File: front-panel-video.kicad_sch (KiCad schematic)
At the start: 0 parts

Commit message: [#81876] Add power section
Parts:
- added J2: DisplayPort-Mini_TE_2129320-3, antmicro-footprints:DisplayPort-Mini_Receptacle_TE_2129320-3, symbol antmicroVideoConnectors:DisplayPort-Mini_TE_2129320-3
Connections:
- new net: J2.1 (GND), J2.13 (GND), J2.14 (GND), J2.19 (GND), J2.7 (GND), J2.8 (GND)
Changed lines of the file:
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@@
+		)
+	)
+	(symbol
+		(lib_id "antmicroVideoConnectors:DisplayPort-Mini_TE_2129320-3")
+		(at 153.67 90.17 0)
+		(unit 1)
+		(exclude_from_sim no)
+		(in_bom yes)
+		(on_board yes)
+		(dnp no)
+		(fields_autoplaced yes)
+		(property "Reference" "J2"
+			(at 166.4335 82.55 0)
+			(effects
+				(font
+					(size 1.27 1.27)
+					(thickness 0.15)
+				)
+			)
+		)
+		(property "Value" "DisplayPort-Mini_TE_2129320-3"
+			(at 199.39 90.17 0)
+			(effects
+				(font
+					(size 1.27 1.27)
+					(thickness 0.15)
+				)
+				(justify left bottom)
+				(hide yes)
+			)
+		)
+		(property "Footprint" "antmicro-footprints:DisplayPort-Mini_Receptacle_TE_2129320-3"
+			(at 199.39 92.71 0)
+			(effects
+				(font
+					(size 1.27 1.27)
+					(thickness 0.15)
+				)
+				(justify left bottom)
+				(hide yes)
+			)
+		)
+		(property "Datasheet" "https://www.te.com/usa-en/product-2129320-3.html"
+			(at 199.39 95.25 0)
+			(effects
+				(font
+					(size 1.27 1.27)
+					(thickness 0.15)
+				)
+				(justify left bottom)
+				(hide yes)
+			)
+		)
+		(property "Description" "DisplayPort, Mini Receptacle Connector 20 Position Through Hole, Right Angle"
+			(at 153.67 90.17 0)
+			(effects
+				(font
+					(size 1.27 1.27)
+				)
+				(hide yes)
+			)
+		)
+		(property "MPN" "2129320-3"
+			(at 166.4335 85.09 0)
+			(effects
+				(font
+					(size 1.27 1.27)
+					(thickness 0.15)
+				)
+			)
+		)
+		(property "Manufacturer" "TE Connectivity"
+			(at 199.39 100.33 0)
+			(effects
+				(font
+					(size 1.27 1.27)
+					(thickness 0.15)
+				)
+				(justify left bottom)
+				(hide yes)
+			)
+		)
+		(property "Author" "Antmicro"
+			(at 199.39 102.87 0)
+			(effects
+				(font
+					(size 1.27 1.27)
+					(thickness 0.15)
+				)
+				(justify left bottom)
+				(hide yes)
+			)
+		)
+		(property "License" "Apache-2.0"
+			(at 199.39 105.41 0)
+			(effects
+				(font
+					(size 1.27 1.27)
+					(thickness 0.15)
+				)
+				(justify left bottom)
+				(hide yes)
+			)
+		)
+		(pin "5"
+		)
+		(pin "SH"
+		)
+		(pin "8"
+		)
+		(pin "13"
+		)
+		(pin "19"
+		)
+		(pin "16"
+		)
+		(pin "20"
+		)
+		(pin "15"
+		)
+		(pin "6"
+		)
+		(pin "1"
+		)
+		(pin "11"
+		)
+		(pin "7"
+		)
+		(pin "17"
+		)
+		(pin "14"
+		)
+		(pin "4"
+		)
+		(pin "10"
+		)
+		(pin "2"
+		)
+		(pin "9"
+		)
+		(pin "12"
+		)
+		(pin "18"
+		)
+		(pin "3"
+		)
+		(instances
+			(project ""
+				(path "/5f636c45-3c15-4731-8931-4625e0dab7e4/32de8c9e-be2b-4d78-9d5d-f4e694f2d2e7"
+					(reference "J2")
+					(unit 1)
+				)
+			)
 		)
 	)

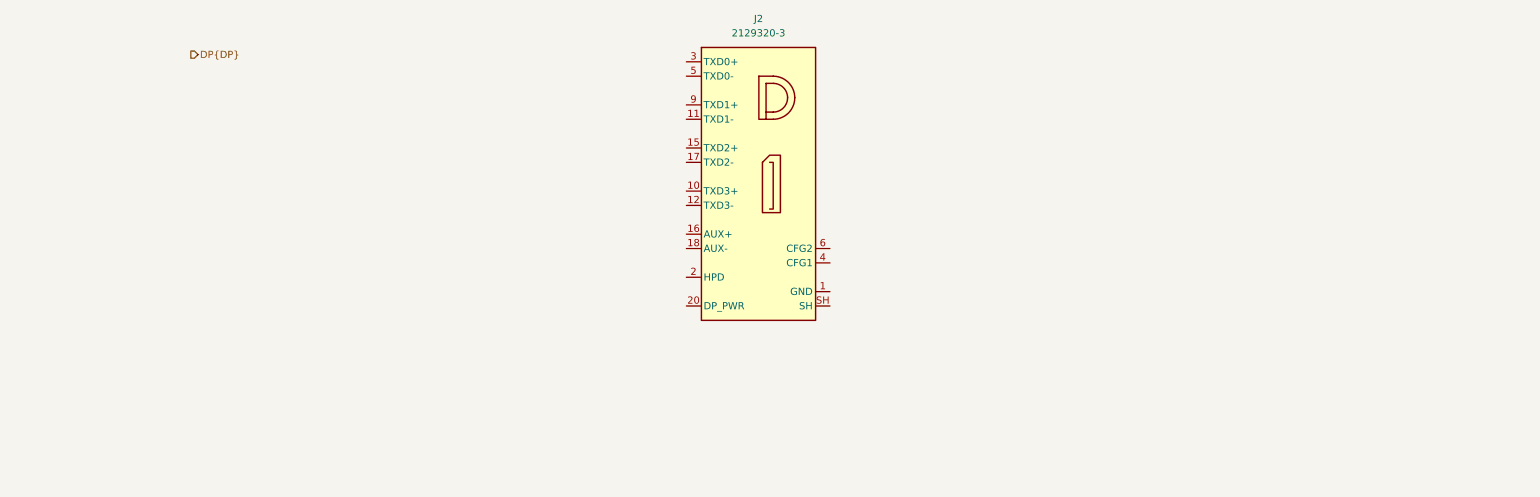
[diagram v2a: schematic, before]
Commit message: [#82153] Add Mini DP passives
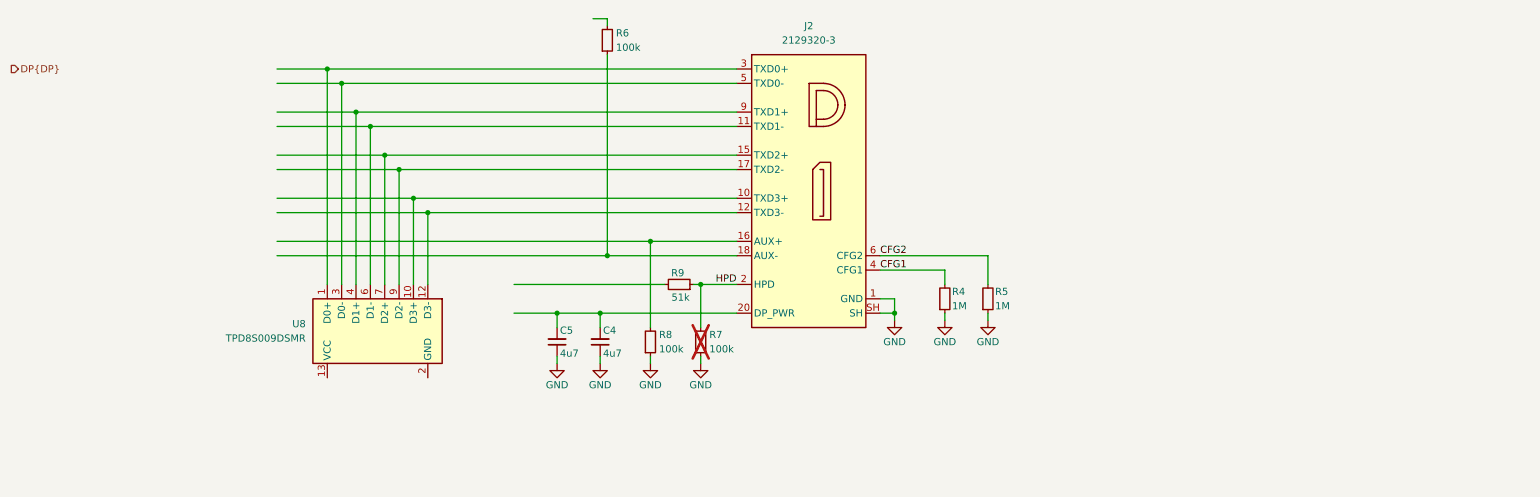
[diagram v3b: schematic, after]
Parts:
- added C4, C5: C_4u7_6.3V_0402, antmicro-footprints:C_0402_1005Metric, symbol antmicroCapacitors0402:C_4u7_6.3V_0402
- added R4, R5: R_1M_0402, antmicro-footprints:R_0402_1005Metric, symbol antmicroResistors0402:R_1M_0402
- added R6, R7, R8: R_100k_0402, antmicro-footprints:R_0402_1005Metric, symbol antmicroResistors0402:R_100k_0402
- added R9: R_51k_0402, antmicro-footprints:R_0402_1005Metric, symbol antmicroResistors0402:R_51k_0402
- added U8: TPD8S009DSMR, antmicro-footprints:R-PDSO-N15, symbol antmicroTVSDiodes:TPD8S009DSMR
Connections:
- net GND: now reaches J2.1 (GND), J2.13 (GND), J2.14 (GND), J2.19 (GND), J2.7 (GND), J2.8 (GND)
- net GND: now also J2.SH, C4.1, C5.1, R4.1, R5.1, R7.1, R8.1
- net at J2.10 (TXD3+): now also U8.10 (D3+)
- net at J2.11 (TXD1-): now also U8.6 (D1-)
- net at J2.12 (TXD3-): now also U8.12 (D3-)
- net at J2.15 (TXD2+): now also U8.7 (D2+)
- net at J2.16 (AUX+): now also R8.2
- net at J2.17 (TXD2-): now also U8.9 (D2-)
- net at J2.18 (AUX-): now also R6.1
- net HPD: now reaches J2.2 (HPD)
- net HPD: now also R7.2, R9.1
- net at J2.20 (DP_PWR): now also C4.2, C5.2
- net at J2.3 (TXD0+): now also U8.1 (D0+)
- net CFG1: now reaches J2.4 (CFG1)
- net CFG1: now also R4.2
- net at J2.5 (TXD0-): now also U8.3 (D0-)
- net CFG2: now reaches J2.6 (CFG2)
- net CFG2: now also R5.2
- net at J2.9 (TXD1+): now also U8.4 (D1+)
- new net: U8.11 (GND), U8.2 (GND), U8.5 (GND), U8.8 (GND)
- new net: U8.13 (VCC), U8.15 (VCC)
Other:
- moved on the sheet: J2

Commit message: [#82153] Finalize video schematic
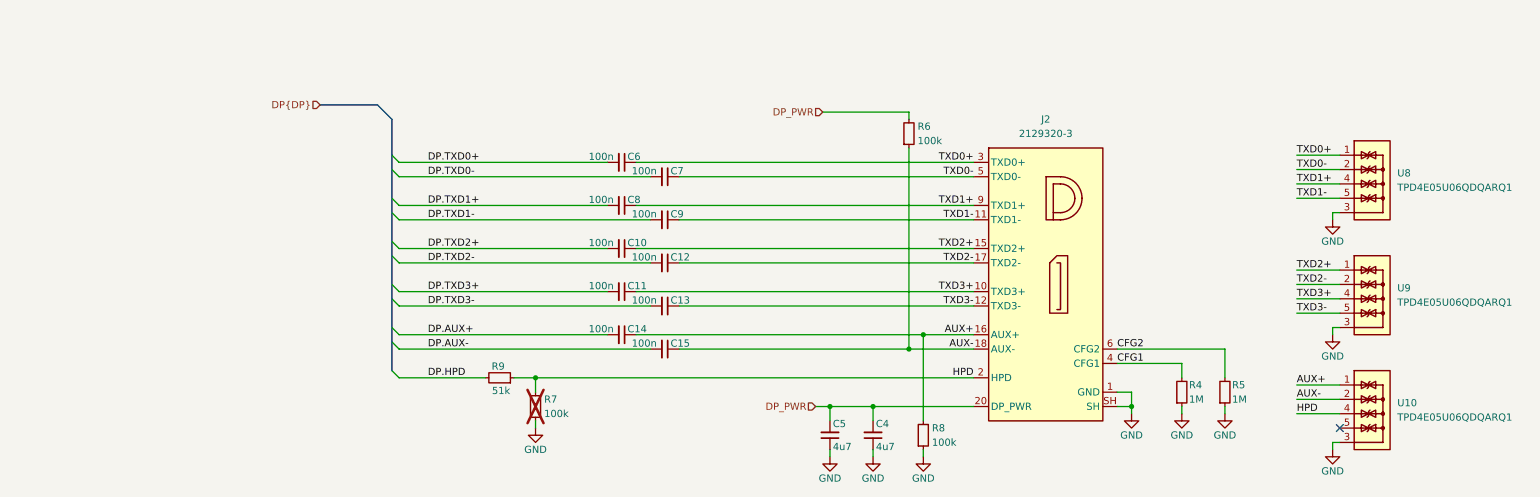
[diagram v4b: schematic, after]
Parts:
- removed U8: TPD8S009DSMR, antmicro-footprints:R-PDSO-N15, symbol antmicroTVSDiodes:TPD8S009DSMR
- added C10, C11, C12, C13, C14, C15, C6, C7, C8, C9: C_100n_0402, antmicro-footprints:C_0402_1005Metric, symbol antmicroCapacitors0402:C_100n_0402
- added U10, U8, U9: TPD4E05U06QDQARQ1, antmicro-footprints:USON-10_2.5x1mm_P0.5mm, symbol antmicroTVSDiodes:TPD4E05U06QDQARQ1
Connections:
- net GND: now also U10.3, U10.8, U8.3, U8.8, U9.3, U9.8
- net HPD: now also U10.4, U10.7
- net AUX-: now reaches J2.18 (AUX-), R6.1
- net AUX-: now also C15.1, U10.2, U10.9
- net DP_PWR: now reaches R6.2
- net DP_PWR: now also C4.2, C5.2, J2.20 (DP_PWR)
- net TXD3+: now reaches J2.10 (TXD3+)
- net TXD3+: now also C11.1, U9.4, U9.7
- net TXD1-: now reaches J2.11 (TXD1-)
- net TXD1-: now also C9.1, U8.5, U8.6
- net TXD3-: now reaches J2.12 (TXD3-)
- net TXD3-: now also C13.1, U9.5, U9.6
- net TXD2+: now reaches J2.15 (TXD2+)
- net TXD2+: now also C10.1, U9.1, U9.10
- net AUX+: now reaches J2.16 (AUX+), R8.2
- net AUX+: now also C14.1, U10.1, U10.10
- net TXD2-: now reaches J2.17 (TXD2-)
- net TXD2-: now also C12.1, U9.2, U9.9
- net TXD0+: now reaches J2.3 (TXD0+)
- net TXD0+: now also C6.1, U8.1, U8.10
- net TXD0-: now reaches J2.5 (TXD0-)
- net TXD0-: now also C7.1, U8.2, U8.9
- net TXD1+: now reaches J2.9 (TXD1+)
- net TXD1+: now also C8.1, U8.4, U8.7
- net DP.HPD: now reaches R9.2
- new net: U10.5, U10.6
- new net DP.AUX+: C14.2
- new net DP.AUX-: C15.2
- new net DP.TXD0+: C6.2
- new net DP.TXD0-: C7.2
- new net DP.TXD1+: C8.2
- new net DP.TXD1-: C9.2
- new net DP.TXD2+: C10.2
- new net DP.TXD2-: C12.2
- new net DP.TXD3+: C11.2
- new net DP.TXD3-: C13.2
- no-connect marks 0 -> 1
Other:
- moved on the sheet: C4, C5, J2, R4, R5, R6, R7, R8, R9

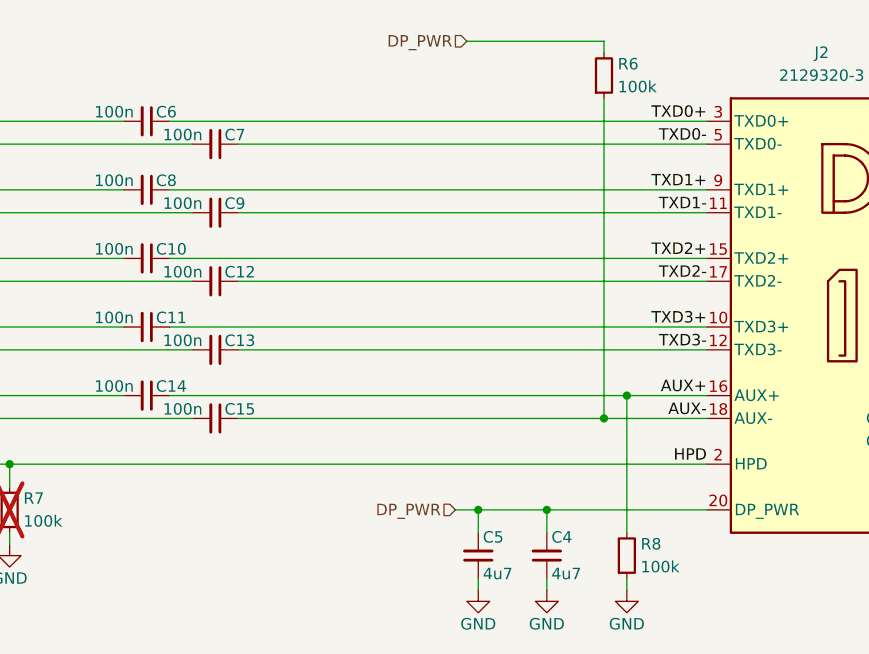
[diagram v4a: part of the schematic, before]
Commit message: [#82157] Add diode to DP_PWR
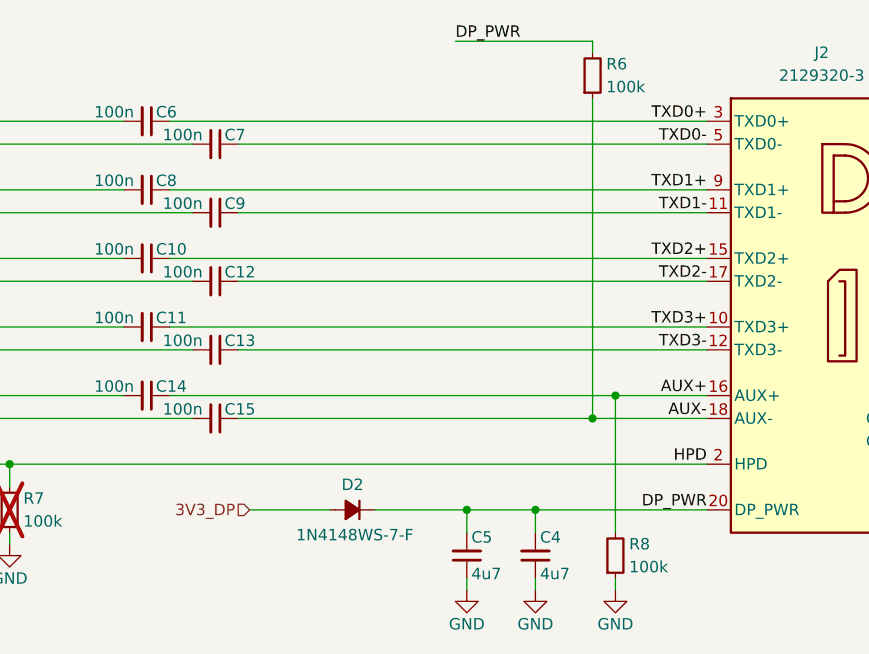
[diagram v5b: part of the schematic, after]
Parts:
- added D2: 1N4148WS-7-F, antmicro-footprints:D_SOD-323, symbol antmicroDiodesRectifiersSingle:1N4148WS-7-F
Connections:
- net DP_PWR: now also D2.1 (C)
- new net 3V3_DP: D2.2 (A)
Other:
- moved on the sheet: C4, C5, R6, R8

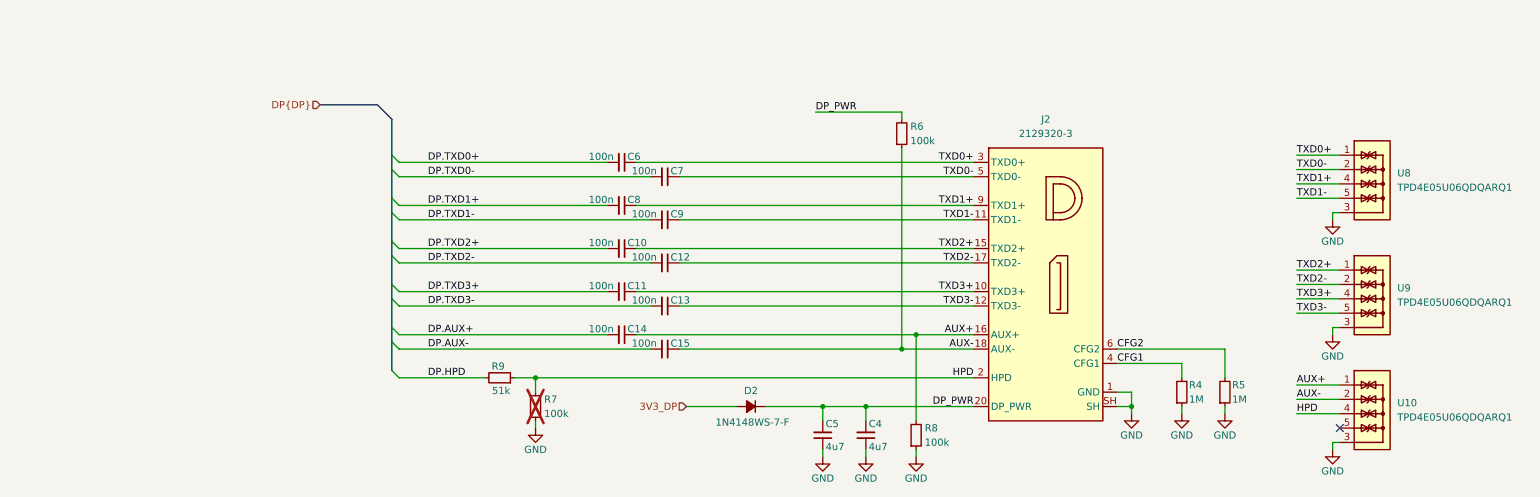
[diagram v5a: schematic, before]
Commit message: [#82176] Fix conflicting annotations
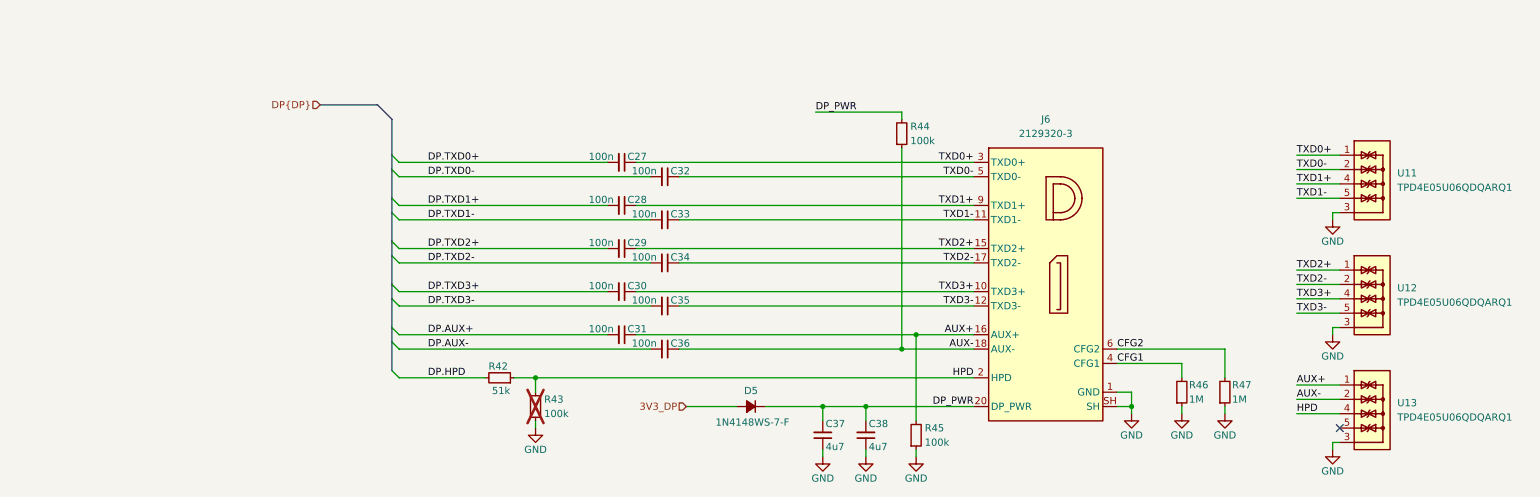
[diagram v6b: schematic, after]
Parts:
- renumbered C6 to C27, C8 to C28, C10 to C29, C11 to C30, C14 to C31, C7 to C32, C9 to C33, C12 to C34, C13 to C35, C15 to C36, C5 to C37, C4 to C38, D2 to D5, J2 to J6, R9 to R42, R7 to R43, R6 to R44, R8 to R45, R4 to R46, R5 to R47, U8 to U11, U9 to U12, U10 to U13
